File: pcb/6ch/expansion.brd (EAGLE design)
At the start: 62 x 42 mm, 48 parts, among them IC3 STM32F042F4, J7 AUDIO_JACK_3.5MM_PTH, J8 AUDIO_JACK_3.5MM_PTH, SW3 324_SW, SW4 324_SW, U1 USBC_16P, U2 USBC_16P, U4 XC6206_DEV

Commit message: added PB1 LED
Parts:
- removed JP1: (no value), adafruit_changed:1X01-CLEANBIG
- added LED8: (no value), adafruit:CHIP-LED0805
- added R19, R20: 5K1, joyAnalog:0805
- added U$2: PINHD1X2, adafruit_changed:1X02
- moved U$3 0.13 mm to (16.4, 12.6)
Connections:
- new net N$9: LED8.A, R20.2
- net +3V3: now also R19.2, R20.1
- net CH_PB1: now also LED8.C, R19.1, U$2.2; no longer JP1.1
- net GND: now also U$2.1
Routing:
- net +3V3: track 219.1 -> 234.1 mm, vias 11 -> 12
- net CH_PB1: track 26.7 -> 35.0 mm
- net N$9: track 0.00 -> 1.91 mm
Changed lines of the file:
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@@
 <text x="30.7052" y="6.1814" size="2.1082" layer="26" rot="MR0" align="center">dekuNukem 2024</text>
 <text x="36.8012" y="21.0404" size="2.1082" layer="26" rot="MR0" align="center">duckyPad.com</text>
-<text x="2.0386" y="8.8462" size="1.27" layer="25" rot="R90" align="center">PB1</text>
+<text x="-4.1844" y="5.6712" size="1.27" layer="25" rot="R90" align="center">PB1</text>
 <text x="39.7902" y="15.8884" size="1.778" layer="25" align="center">1</text>
 <text x="22.2642" y="15.8884" size="1.778" layer="25" align="center">6</text>
@@
 <attribute name="VALUE" x="44.958" y="23.749" size="1.27" layer="27" rot="R180"/>
 </element>
-<element name="JP1" library="adafruit_changed" package="1X01-CLEANBIG" value="" x="4.445" y="8.636" smashed="yes">
-<attribute name="VALUE" x="3.175" y="5.461" size="1.27" layer="27"/>
-</element>
 <element name="JP2" library="pinhead" library_urn="urn:adsk.eagle:library:325" package="2X03" package3d_urn="urn:adsk.eagle:package:22462/2" value="" x="59.055" y="11.176" smashed="yes" rot="R270">
 <attribute name="POPULARITY" value="62" x="59.055" y="11.176" size="0.3048" layer="27" rot="R270" display="off"/>
@@
 </element>
 <element name="U$1" library="adafruit_changed" package="1X02" value="PINHD1X2" x="45.593" y="15.875" smashed="yes" rot="R45"/>
-<element name="U$3" library="adafruit_changed" package="1X02" value="PINHD1X2" x="16.383" y="12.446" smashed="yes" rot="R180"/>
+<element name="U$3" library="adafruit_changed" package="1X02" value="PINHD1X2" x="16.383" y="12.573" smashed="yes" rot="R180"/>
+<element name="R19" library="joyAnalog" package="0805" value="5K1" x="4.445" y="8.382" smashed="yes">
+<attribute name="NAME" x="3.556" y="6.6675" size="0.8128" layer="25"/>
+</element>
+<element name="LED8" library="adafruit" package="CHIP-LED0805" value="" x="1.651" y="9.271" smashed="yes" rot="R180">
+<attribute name="VALUE" x="-0.889" y="10.541" size="1.27" layer="27" rot="R270"/>
+</element>
+<element name="R20" library="joyAnalog" package="0805" value="5K1" x="4.445" y="10.287" smashed="yes" rot="R180">
+<attribute name="NAME" x="5.9055" y="11.303" size="0.8128" layer="25" rot="R270"/>
+</element>
+<element name="U$2" library="adafruit_changed" package="1X02" value="PINHD1X2" x="9.271" y="12.573" smashed="yes" rot="R180"/>
 </elements>
 <signals>
@@
 <contactref element="JP2" pad="3"/>
 <contactref element="JP2" pad="4"/>
+<contactref element="U$2" pad="1"/>
 </signal>
 <signal name="+3V3">
@@
 <wire x1="55.383" y1="36.449" x2="55.383" y2="33.909" width="0.3048" layer="1"/>
 <wire x1="55.383" y1="33.909" x2="55.383" y2="31.242" width="0.3048" layer="1"/>
-<wire x1="0.889" y1="34.29" x2="0.889" y2="20.447" width="0.3048" layer="16"/>
-<wire x1="0.889" y1="20.447" x2="1.905" y2="19.431" width="0.3048" layer="16"/>
-<wire x1="1.905" y1="19.431" x2="18.415" y2="19.431" width="0.3048" layer="16"/>
-<wire x1="18.415" y1="19.431" x2="20.193" y2="17.653" width="0.3048" layer="16"/>
+<wire x1="20.193" y1="17.653" x2="18.415" y2="19.431" width="0.3048" layer="16"/>
 <wire x1="20.193" y1="17.653" x2="25.146" y2="17.653" width="0.3048" layer="16"/>
 <wire x1="25.146" y1="17.653" x2="30.099" y2="17.653" width="0.3048" layer="16"/>
@@
 <wire x1="22.86" y1="9.144" x2="22.352" y2="9.144" width="0.2032" layer="16"/>
 <wire x1="25.908" y1="12.192" x2="22.86" y2="9.144" width="0.2032" layer="16"/>
+<contactref element="R19" pad="2"/>
+<contactref element="R20" pad="1"/>
+<wire x1="2.413" y1="11.684" x2="4.445" y2="11.684" width="0.3048" layer="16"/>
+<wire x1="2.413" y1="11.684" x2="0.889" y2="13.208" width="0.3048" layer="16"/>
+<via x="4.445" y="11.684" extent="1-16" drill="0.55"/>
+<wire x1="5.345" y1="11.165" x2="4.826" y2="11.684" width="0.3048" layer="1"/>
+<wire x1="4.445" y1="11.684" x2="4.826" y2="11.684" width="0.3048" layer="1"/>
+<wire x1="5.345" y1="11.165" x2="5.345" y2="10.287" width="0.3048" layer="1"/>
+<wire x1="0.889" y1="34.29" x2="0.889" y2="19.431" width="0.3048" layer="16"/>
+<wire x1="0.889" y1="19.431" x2="0.889" y2="13.208" width="0.3048" layer="16"/>
+<wire x1="5.345" y1="10.287" x2="5.345" y2="8.382" width="0.3048" layer="1"/>
+<wire x1="18.415" y1="19.431" x2="0.889" y2="19.431" width="0.3048" layer="16"/>
 </signal>
 <signal name="USBDP/U1RX">
@@
 <contactref element="U$3" pad="2"/>
 <wire x1="28.5782" y1="5.614" x2="23.596" y2="5.614" width="0.2032" layer="1"/>
-<wire x1="18.669" y1="10.541" x2="17.018" y2="10.541" width="0.2032" layer="1"/>
-<wire x1="17.018" y1="10.541" x2="15.113" y2="12.446" width="0.2032" layer="1"/>
+<wire x1="18.669" y1="10.541" x2="17.145" y2="10.541" width="0.2032" layer="1"/>
+<wire x1="17.145" y1="10.541" x2="15.113" y2="12.573" width="0.2032" layer="1"/>
 <wire x1="23.596" y1="5.614" x2="18.669" y2="10.541" width="0.2032" layer="1"/>
-<wire x1="15.113" y1="12.446" x2="10.287" y2="17.272" width="0.2032" layer="1"/>
-<wire x1="10.287" y1="17.272" x2="10.287" y2="20.25" width="0.2032" layer="1"/>
+<wire x1="15.113" y1="12.573" x2="10.287" y2="17.399" width="0.2032" layer="1"/>
+<wire x1="10.287" y1="17.399" x2="10.287" y2="20.25" width="0.2032" layer="1"/>
 </signal>
 <signal name="N$31">
@@
 <wire x1="7.6575" y1="19.25" x2="8.817" y2="19.25" width="0.2032" layer="1"/>
 <wire x1="8.817" y1="19.25" x2="9.144" y2="18.923" width="0.2032" layer="1"/>
-<wire x1="9.144" y1="18.923" x2="9.144" y2="15.748" width="0.2032" layer="1"/>
-<wire x1="7.239" y1="13.843" x2="5.599" y2="13.843" width="0.2032" layer="1"/>
-<wire x1="9.144" y1="15.748" x2="7.239" y2="13.843" width="0.2032" layer="1"/>
+<wire x1="9.144" y1="18.923" x2="9.144" y2="16.383" width="0.2032" layer="1"/>
+<wire x1="6.604" y1="13.843" x2="5.599" y2="13.843" width="0.2032" layer="1"/>
+<wire x1="9.144" y1="16.383" x2="6.604" y2="13.843" width="0.2032" layer="1"/>
 </signal>
 <signal name="N$33">
@@
 <contactref element="U$3" pad="1"/>
 <wire x1="28.5782" y1="6.264" x2="23.962" y2="6.264" width="0.2032" layer="1"/>
-<wire x1="17.78" y1="12.446" x2="17.653" y2="12.446" width="0.2032" layer="1"/>
-<wire x1="23.962" y1="6.264" x2="17.78" y2="12.446" width="0.2032" layer="1"/>
-<wire x1="17.653" y1="12.446" x2="11.303" y2="18.796" width="0.2032" layer="1"/>
-<wire x1="11.303" y1="18.796" x2="11.303" y2="20.955" width="0.2032" layer="1"/>
+<wire x1="23.962" y1="6.264" x2="17.653" y2="12.573" width="0.2032" layer="1"/>
+<wire x1="17.653" y1="12.573" x2="11.303" y2="18.923" width="0.2032" layer="1"/>
+<wire x1="11.303" y1="18.923" x2="11.303" y2="20.955" width="0.2032" layer="1"/>
 </signal>
 <signal name="+5V">
@@
 <wire x1="26.797" y1="8.763" x2="27.346" y2="8.214" width="0.2032" layer="1"/>
 <wire x1="27.346" y1="8.214" x2="28.5782" y2="8.214" width="0.2032" layer="1"/>
-<contactref element="JP1" pad="1"/>
 <wire x1="9.27" y1="6.477" x2="8" y2="7.747" width="0.2032" layer="16"/>
 <wire x1="8" y1="7.747" x2="8" y2="8.556" width="0.2032" layer="16"/>
-<wire x1="4.445" y1="8.636" x2="7.92" y2="8.636" width="0.2032" layer="16"/>
-<wire x1="7.92" y1="8.636" x2="8" y2="8.556" width="0.2032" layer="16"/>
+<contactref element="R19" pad="1"/>
+<contactref element="LED8" pad="C"/>
+<wire x1="1.651" y1="8.221" x2="3.384" y2="8.221" width="0.2032" layer="1"/>
+<wire x1="3.384" y1="8.221" x2="3.545" y2="8.382" width="0.2032" layer="1"/>
+<wire x1="3.545" y1="8.382" x2="3.545" y2="8.012" width="0.2032" layer="1"/>
+<wire x1="6.429" y1="6.985" x2="8" y2="8.556" width="0.2032" layer="1"/>
+<wire x1="3.545" y1="8.012" x2="4.572" y2="6.985" width="0.2032" layer="1"/>
+<wire x1="4.572" y1="6.985" x2="6.429" y2="6.985" width="0.2032" layer="1"/>
+<contactref element="U$2" pad="2"/>
+<wire x1="8.001" y1="12.573" x2="8.001" y2="8.557" width="0.3048" layer="16"/>
+<wire x1="8.001" y1="8.557" x2="8" y2="8.556" width="0.3048" layer="16"/>
 </signal>
 <signal name="CH_PF0">
@@
 <wire x1="44.738" y1="19.2" x2="44.588" y2="19.05" width="0.2032" layer="1"/>
 </signal>
+<signal name="N$9">
+<contactref element="LED8" pad="A"/>
+<contactref element="R20" pad="2"/>
+<wire x1="1.651" y1="10.321" x2="3.511" y2="10.321" width="0.2032" layer="1"/>
+<wire x1="3.511" y1="10.321" x2="3.545" y2="10.287" width="0.2032" layer="1"/>
+</signal>
 </signals>

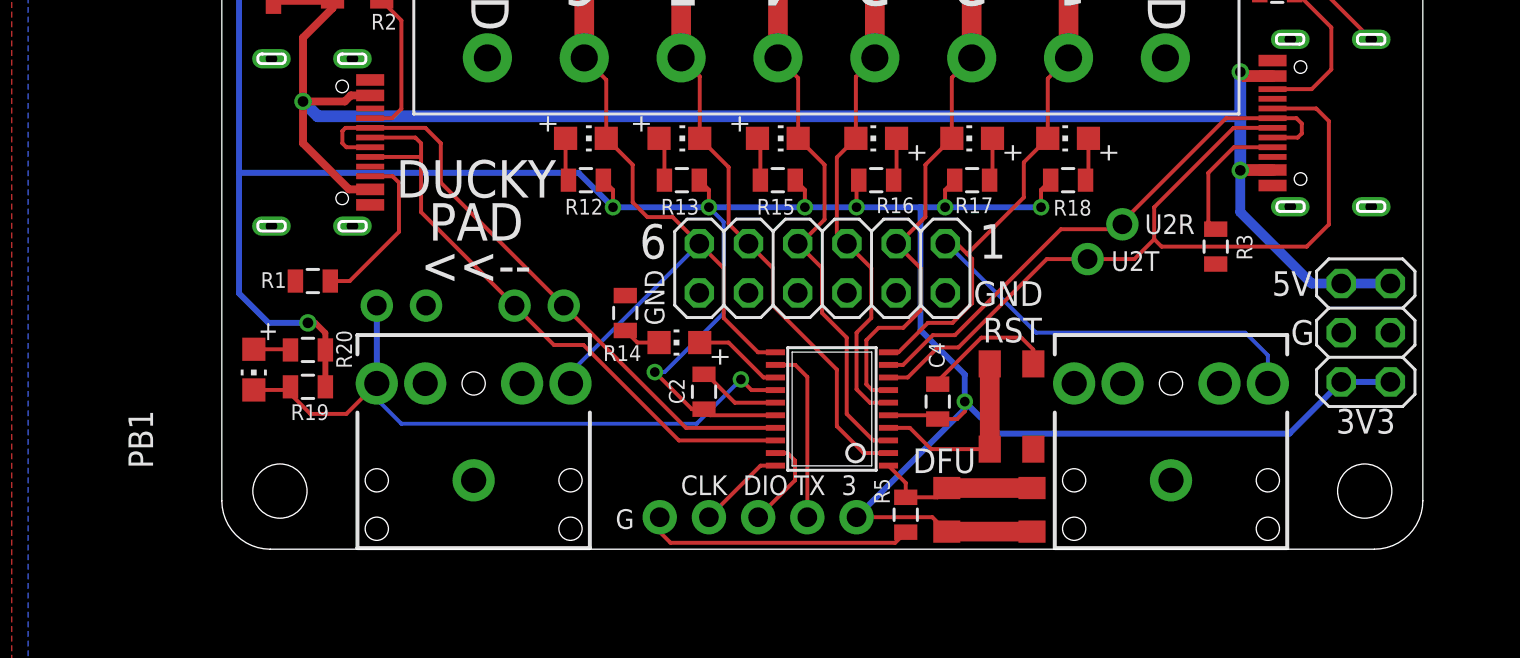
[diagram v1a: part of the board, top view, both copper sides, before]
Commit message: added 2 aux channels, cleanup
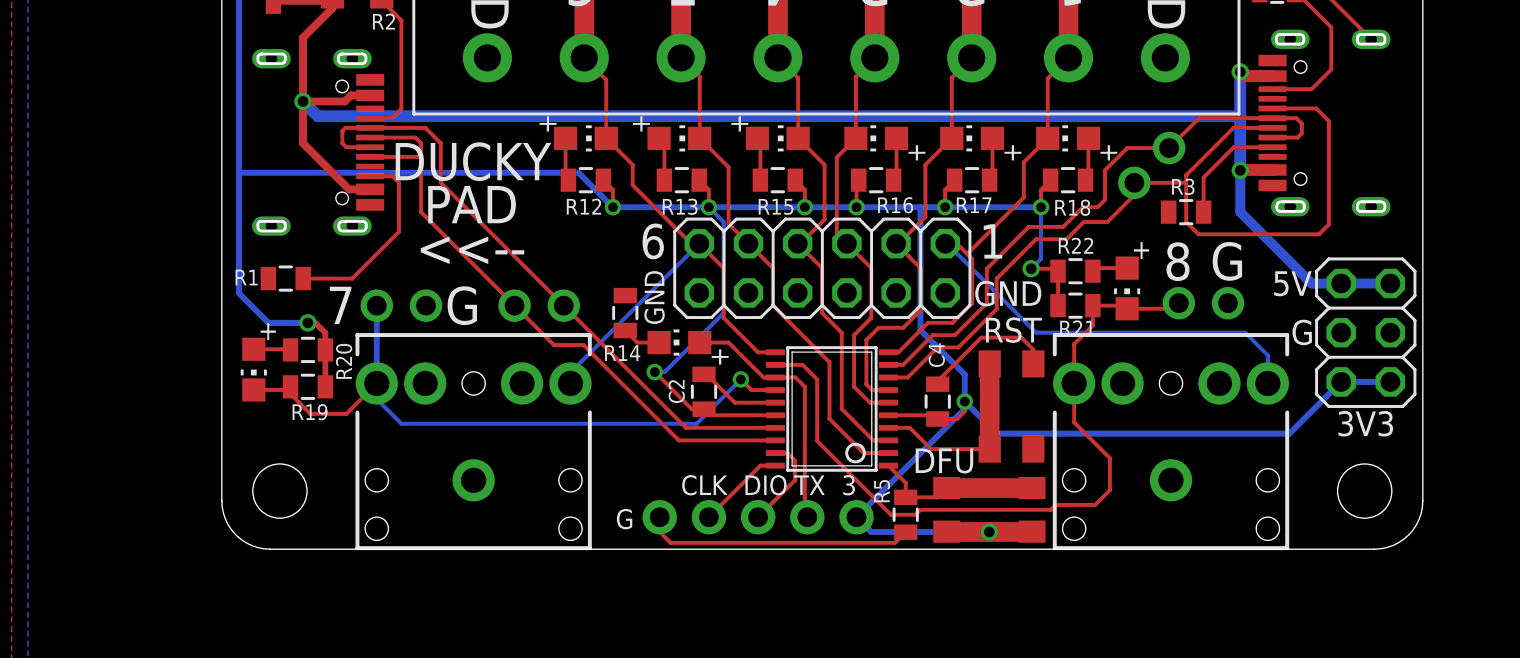
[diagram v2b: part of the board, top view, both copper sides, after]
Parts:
- added LED9: (no value), adafruit:CHIP-LED0805
- added R21, R22: 5K1, joyAnalog:0805
- added U$4: PINHD1X2, adafruit_changed:1X02
- moved U$1 4.62 mm to (48.0, 19.8)
- moved R3 2.34 mm to (49.8, 17.4), turned to 180 degrees
- moved R1 1.40 mm to (3.30, 14.0)
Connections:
- removed net N$14: IC3.12, U$6.4
- new net CH_PA6: IC3.12, J8.RING, LED9.C, R21.1, U$4.2
- new net N$10: IC3.13, LED3.A, U$6.4
- net +3V3: now also R21.2, R22.1
- net GND: now also U$4.1
- net N$12: now also LED9.A, R22.2; no longer IC3.13, LED3.A
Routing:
- net CH_PA6: track 0.00 -> 38.2 mm
- net N$10: track 0.00 -> 13.2 mm
- net N$14: track 9.15 -> 0.00 mm
- net +3V3: track 234.1 -> 242.9 mm, vias 12 -> 14
- net N$12: track 4.65 -> 1.83 mm
- net U2RX: track 28.9 -> 30.8 mm
- net N$31: track 8.76 -> 10.1 mm
- net N$1: track 6.93 -> 5.99 mm
- net U2TX: track 44.3 -> 45.1 mm
- net CH_PA5: track 50.5 -> 49.9 mm
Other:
- board text added: "7"
- board text added: "8"
- board text removed: "PB1"
- board text removed: "U2R"
- board text removed: "U2T"

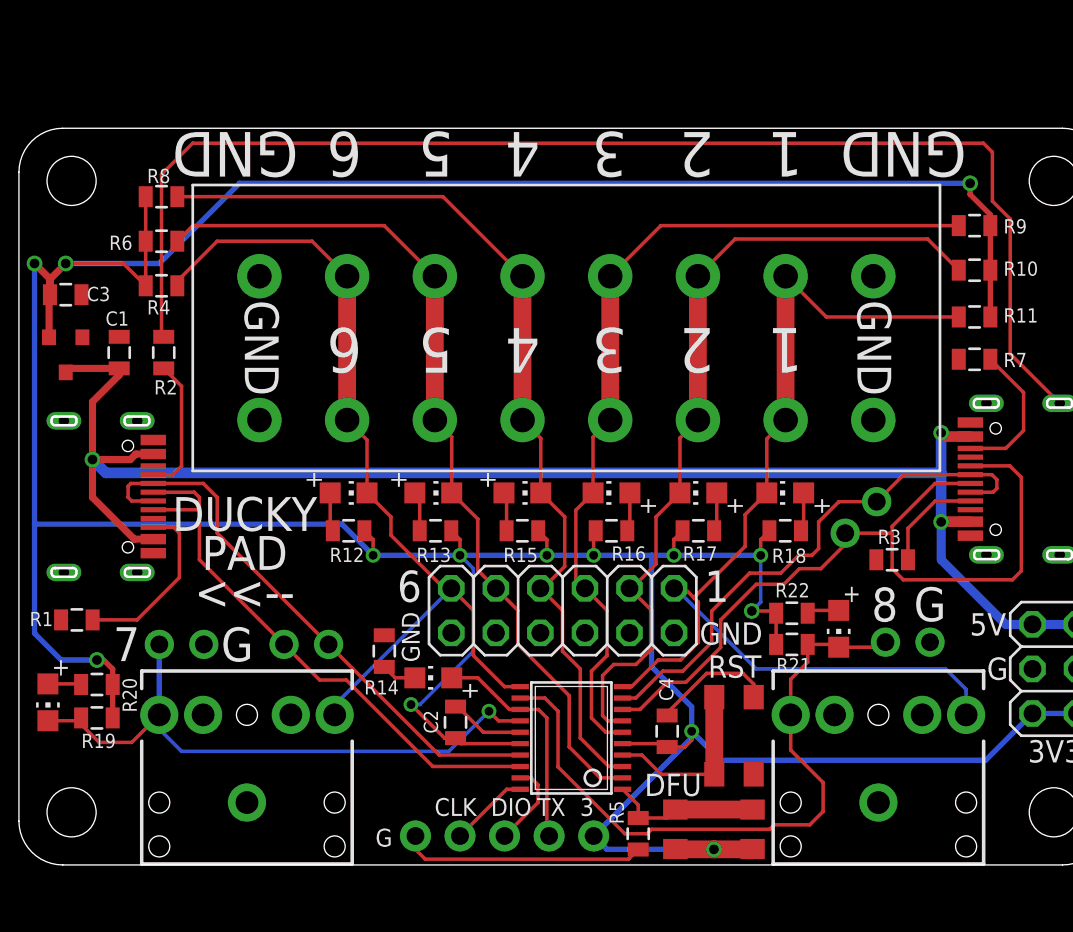
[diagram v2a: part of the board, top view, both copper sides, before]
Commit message: moved channel 7 to terminal and on header
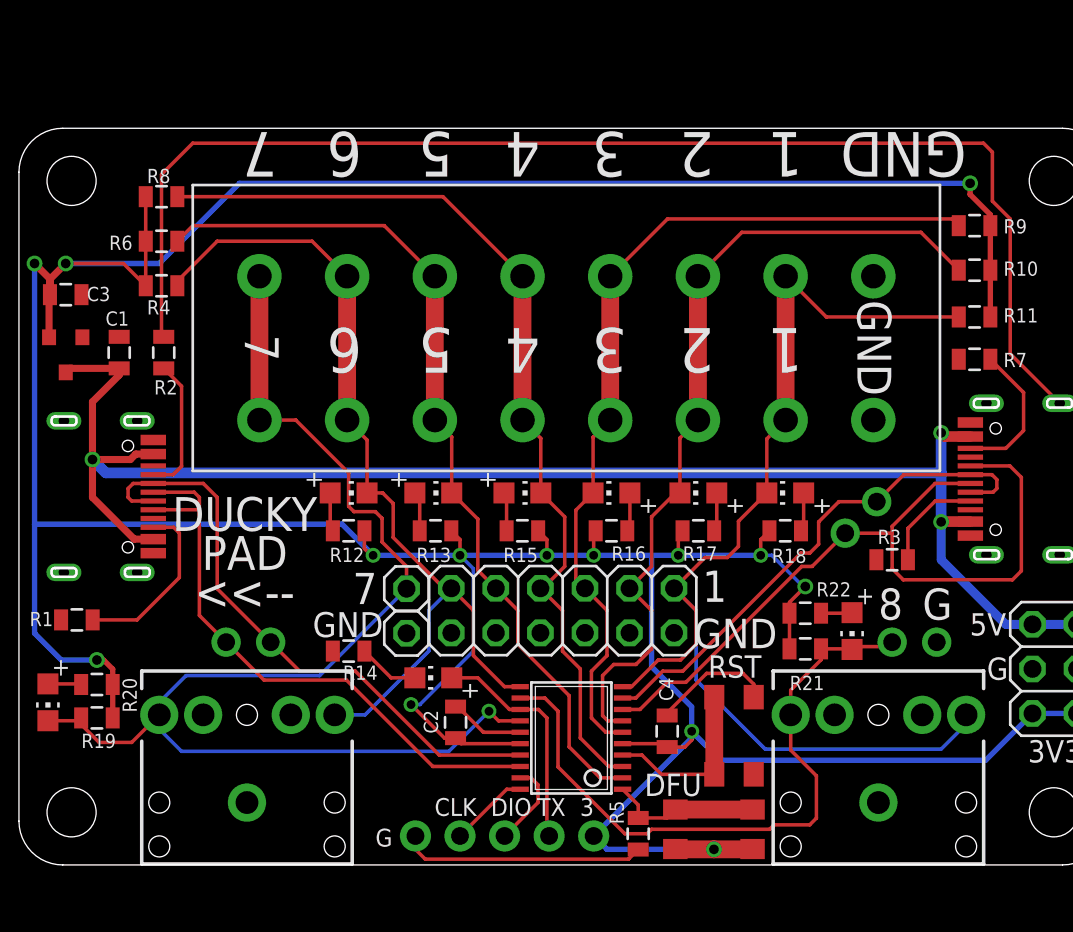
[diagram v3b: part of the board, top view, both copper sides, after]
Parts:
- removed U$4: PINHD1X2, adafruit_changed:1X02
- added JP1, JP3: (no value), pinhead:1X01
- moved U$2 41.8 mm to (51.1, 12.7), turned to 0 degrees
- moved U$3 3.30 mm to (13.1, 12.7)
- moved R14 2.03 mm to (18.8, 12.2), turned to 0 degrees
- moved R21 0.80 mm to (44.8, 12.3)
- moved LED9 0.77 mm to (47.5, 13.3)
- moved R22 0.76 mm to (44.8, 14.4)
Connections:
- net CH_PA6: now also U$2.1; no longer U$4.2
- net CH_PB1: now also JP1.1, U$14.P$1, U$14.P$2; no longer U$2.2
- net GND: now also JP3.1, U$2.2; no longer U$14.P$1, U$14.P$2, U$2.1, U$4.1
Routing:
- net CH_PB1: track 35.0 -> 71.7 mm
- net CH_PA4: track 61.2 -> 64.8 mm
- net USBDP/U1RX: track 32.1 -> 34.0 mm
- net USBDN/U1TX: track 32.2 -> 34.0 mm
- net CH_PA5: track 49.9 -> 51.5 mm
- net N$11: track 2.00 -> 3.51 mm
- net U2TX: track 45.1 -> 43.8 mm
- net U2RX: track 30.8 -> 29.6 mm
- net CH_PA6: track 38.2 -> 37.5 mm
- net +3V3: track 242.9 -> 243.4 mm
